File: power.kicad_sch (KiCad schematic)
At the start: 15 parts

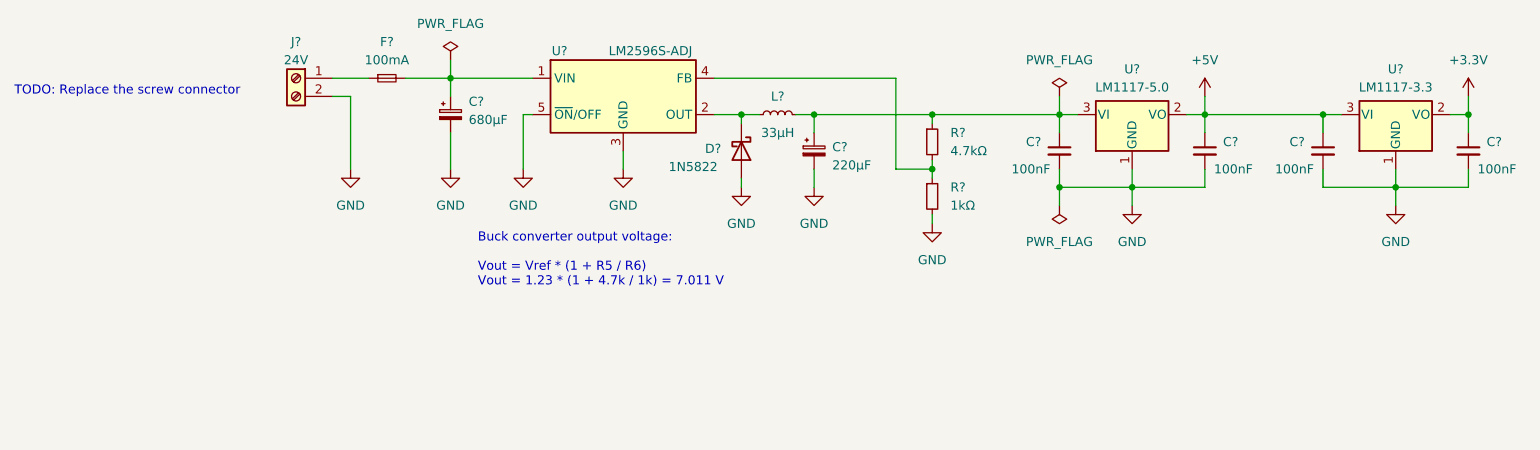
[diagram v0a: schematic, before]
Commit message: Refactor the mainboard
- Use smaller STM
- Use MPU-9250 as a motion sensor
- Connect some peripherals to the MCU
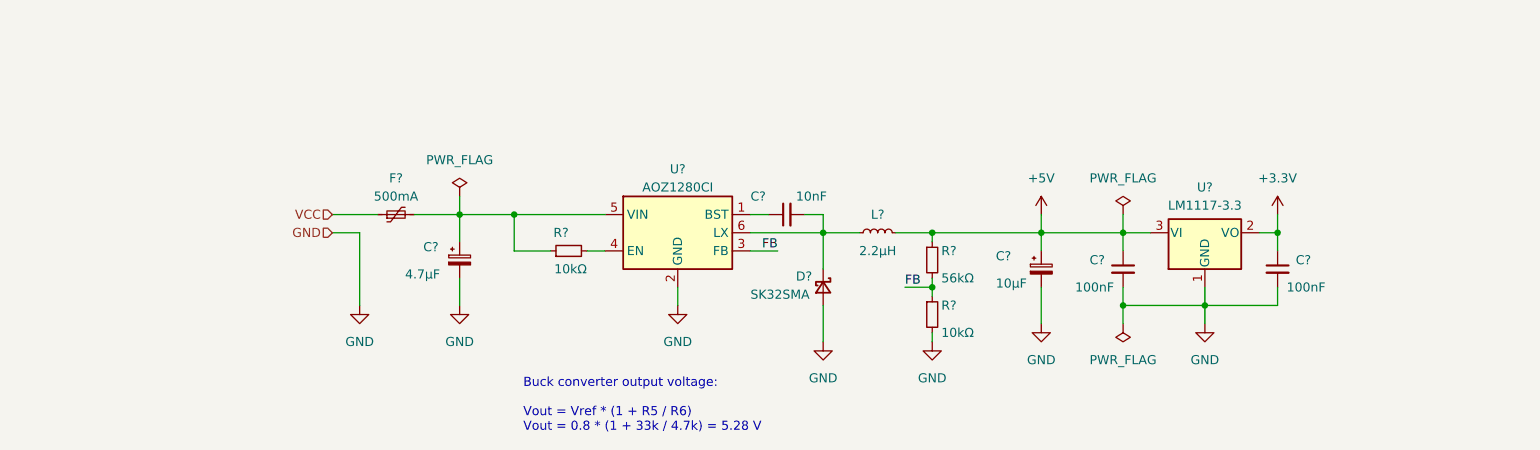
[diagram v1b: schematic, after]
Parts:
- removed C? (x4): 100nF, symbol Device:C_Small
- removed C?: 680μF, symbol Device:C_Polarized_Small
- removed C?: 220μF, symbol Device:C_Polarized_Small
- removed D?: 1N5822, Diode_THT:D_DO-201AD_P15.24mm_Horizontal, symbol Diode:1N5822
- removed F?: 100mA, symbol Device:Fuse_Small
- removed J?: 24V, symbol Connector:Screw_Terminal_01x02
- removed L?: 33μH, symbol Device:L_Small
- removed R?: 1kΩ, symbol Device:R_Small
- removed R?: 4.7kΩ, symbol Device:R_Small
- removed U?: LM1117-3.3, symbol Regulator_Linear:LM1117-3.3
- removed U?: LM2596S-ADJ, Package_TO_SOT_SMD:TO-263-5_TabPin3, symbol Regulator_Switching:LM2596S-ADJ
- removed U?: LM1117-5.0, symbol Regulator_Linear:LM1117-5.0
- added C? (x2): 100nF, Capacitor_SMD:C_0603_1608Metric, symbol Device:C_Small
- added C?: 10μF, Capacitor_SMD:C_Elec_4x5.4, symbol Device:C_Polarized_Small
- added C?: 10nF, Capacitor_SMD:C_0603_1608Metric, symbol Device:C_Small
- added C?: 4.7μF, Capacitor_SMD:C_Elec_4x5.4, symbol Device:C_Polarized_Small
- added D?: SK32SMA, Diode_SMD:D_SMA, symbol Device:D_Schottky_Small
- added F?: 500mA, Fuse:Fuse_1210_3225Metric, symbol Device:Polyfuse_Small
- added L?: 2.2μH, Inductor_SMD:L_Bourns-SRN4018, symbol Device:L_Small
- added R? (x2): 10kΩ, Resistor_SMD:R_0603_1608Metric, symbol Device:R_Small
- added R?: 56kΩ, Resistor_SMD:R_0603_1608Metric, symbol Device:R_Small
- added U?: LM1117-3.3, Package_TO_SOT_SMD:SOT-223-3_TabPin2, symbol Regulator_Linear:LM1117-3.3
- added U?: AOZ1280CI, Package_TO_SOT_SMD:SOT-23-6, symbol Regulator_Switching:AOZ1280CI
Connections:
- net +3.3V: now also C?.1, U?.2 (VO)
- net +5V: now also C?.1, C?.1, L?.2, R?.1, U?.3 (VI)
- net GND: now also C?.2, C?.2, C?.2, C?.2, D?.2 (A), R?.2, U?.1 (GND), U?.2 (GND)
- new net: C?.1, F?.2, R?.1, U?.5 (VIN)
- new net: R?.2, U?.4 (EN)
- new net: C?.1, U?.1 (BST)
- new net: C?.2, D?.1 (K), L?.1, U?.6 (LX)
- new net FB: R?.1, R?.2, U?.3 (FB)
- new net VCC: F?.1
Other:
- note added: "Buck converter output voltage: Vout = Vref * (1 + R5 / R6) Vout = 0.8 * (1 + 33k / 4.7k) = 5.28 V"
- note removed: "Buck converter output voltage: Vout = Vref * (1 + R5 / R6) Vout = 1.23 * (1 + 4.7k / 1k) = 7.011 V"
- note removed: "TODO: Replace the screw connector"

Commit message: Connect sensors to the MCU
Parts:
- added SW2: POWER, symbol Switch:SW_SPST
- gave numbers to parts that had none: 13
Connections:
- net at C13.1, R4.1, U4.5 (VIN): now also SW2.2 (B); no longer F1.2
- new net: F1.2, SW2.1 (A)
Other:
- moved on the sheet: F1

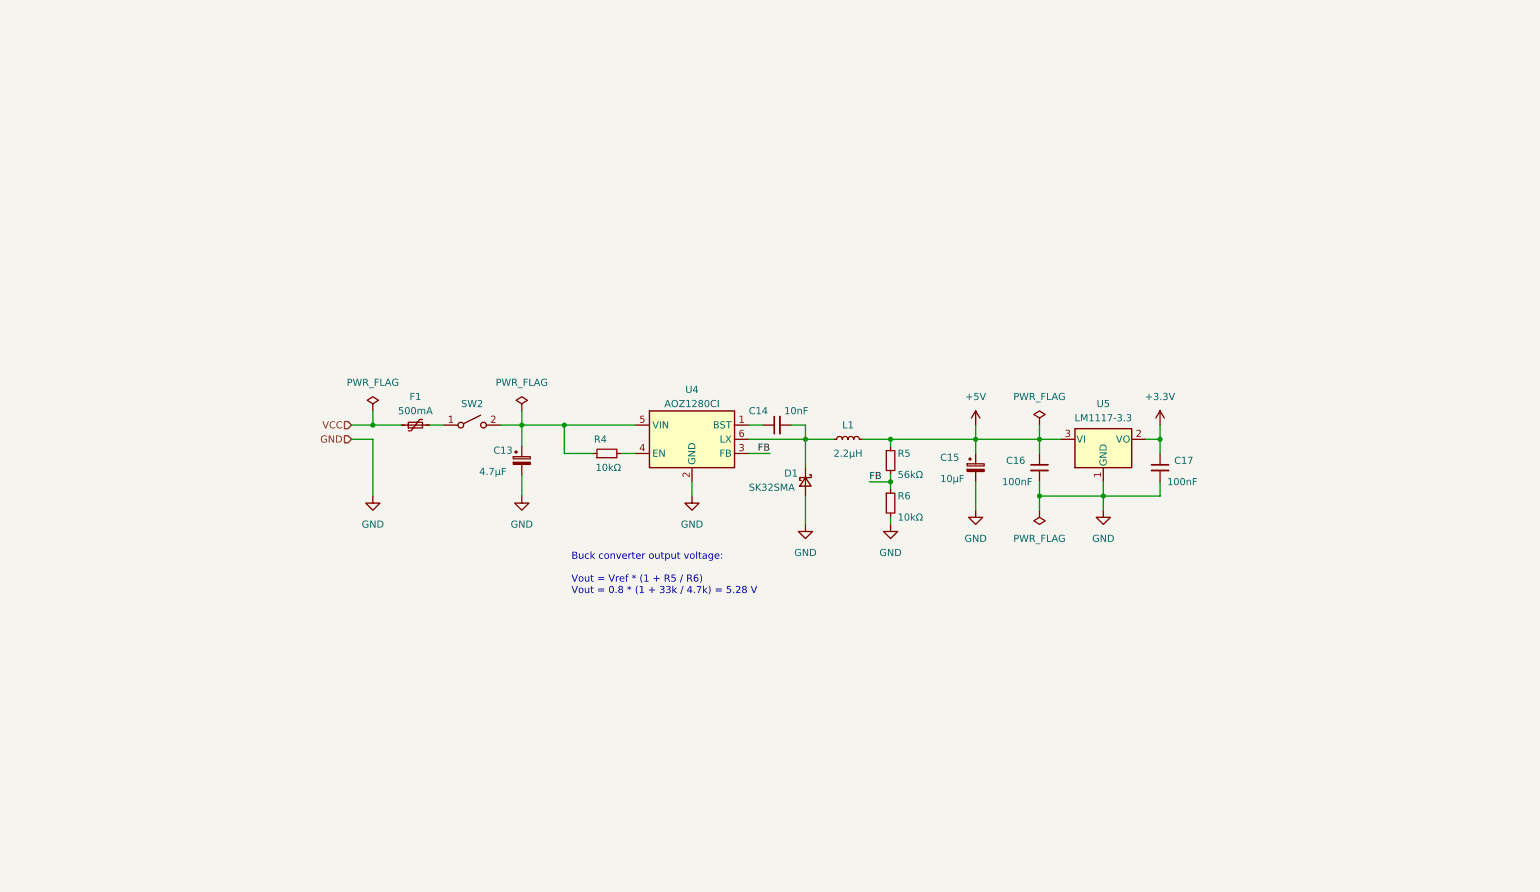
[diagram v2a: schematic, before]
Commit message: Improve the power section:
- add ADC circuit to measure battery level
- add 5V LDO regulator
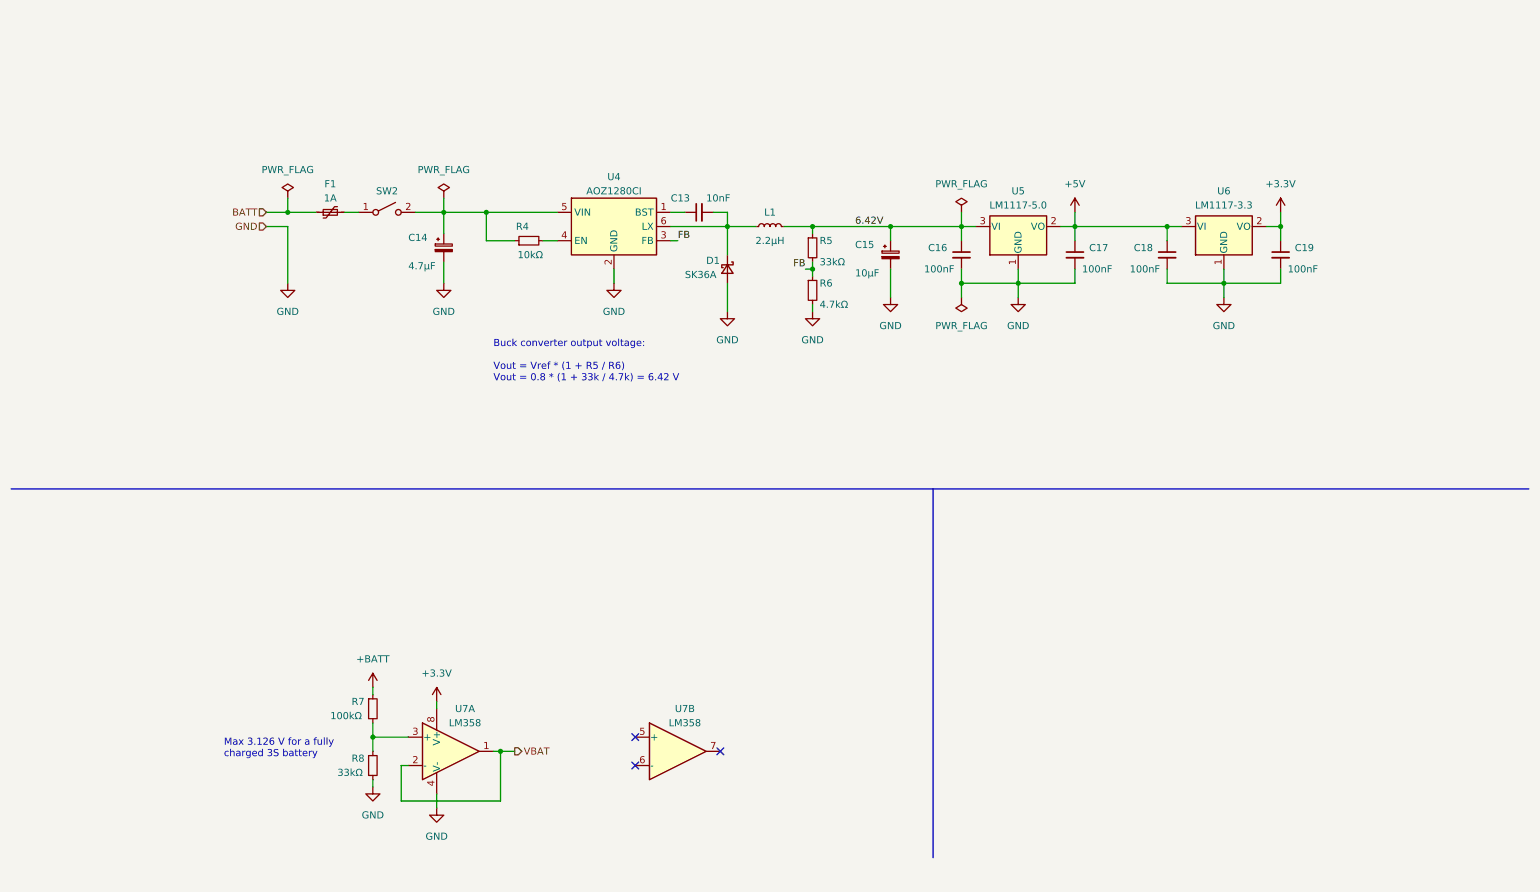
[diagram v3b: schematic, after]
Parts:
- removed C13: 4.7μF, Capacitor_SMD:C_Elec_4x5.4, symbol Device:C_Polarized_Small
- removed C14: 10nF, Capacitor_SMD:C_0603_1608Metric, symbol Device:C_Small
- removed U5: LM1117-3.3, Package_TO_SOT_SMD:SOT-223-3_TabPin2, symbol Regulator_Linear:LM1117-3.3
- added C13: 10nF, Capacitor_SMD:C_0603_1608Metric, symbol Device:C_Small
- added C14: 4.7μF, Capacitor_SMD:CP_Elec_6.3x5.4, symbol Device:C_Polarized_Small
- added C18, C19: 100nF, Capacitor_SMD:C_0603_1608Metric, symbol Device:C_Small
- added R7: 100kΩ, symbol Device:R_Small
- added R8: 33kΩ, symbol Device:R_Small
- added U5: LM1117-5.0, Package_TO_SOT_SMD:SOT-223-3_TabPin2, symbol Regulator_Linear:LM1117-5.0
- added U6: LM1117-3.3, Package_TO_SOT_SMD:SOT-223-3_TabPin2, symbol Regulator_Linear:LM1117-3.3
- added U7: LM358, symbol Amplifier_Operational:LM358
- C15: footprint Capacitor_SMD:C_Elec_4x5.4 -> Capacitor_SMD:CP_Elec_6.3x5.4
- D1: value SK32SMA -> SK36A
- F1: value 500mA -> 1A
- R5: value 56kΩ -> 33kΩ
- R6: value 10kΩ -> 4.7kΩ
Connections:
- net +3.3V: now also C19.1, U6.2 (VO), U7.8 (V+); no longer C17.1
- net +5V: now also C17.1, C18.1, U5.2 (VO), U6.3 (VI); no longer C15.1, C16.1, L1.2, R5.1
- net GND: now also C14.2, C18.2, C19.2, R8.2, U5.1 (GND), U6.1 (GND), U7.4 (V-)
- net at R4.1, SW2.2 (B), U4.5 (VIN): now also C14.1
- net at U4.1 (BST): now also C13.1
- net at D1.1 (K), L1.1, U4.6 (LX): now also C13.2
- net VCC renamed BATT
- new net: R7.2, R8.1, U7.3 (+)
- new net +BATT: R7.1
- new net 6.42V: C15.1, C16.1, L1.2, R5.1, U5.3 (VI)
- new net VBAT: U7.1, U7.2 (-)
- no-connect marks 0 -> 3
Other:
- note added: "Buck converter output voltage: Vout = Vref * (1 + R5 / R6) Vout = 0.8 * (1 + 33k / 4.7k) = 6.42 V"
- note added: "Max 3.126 V for a fully charged 3S battery"
- note removed: "Buck converter output voltage: Vout = Vref * (1 + R5 / R6) Vout = 0.8 * (1 + 33k / 4.7k) = 5.28 V"
- title: (none) -> Power Supply

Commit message: Assign footprints to symbols
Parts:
- removed SW2: POWER, symbol Switch:SW_SPST
- removed U7: LM358, symbol Amplifier_Operational:LM358
- added U5: LM358, Package_SO:SOIC-8_3.9x4.9mm_P1.27mm, symbol Amplifier_Operational:LM358
- R10: renamed from R8; footprint (none) -> Resistor_SMD:R_0603_1608Metric
- R9: renamed from R7; footprint (none) -> Resistor_SMD:R_0603_1608Metric
- renumbered C14 to C10, C15 to C11, C16 to C12, C17 to C13, C18 to C14, C19 to C15, C13 to C9, R4 to R6, R5 to R7, R6 to R8, U4 to U2, U5 to U3, U6 to U4
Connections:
- net +3.3V: now also U5.8 (V+)
- net GND: now also U5.4 (V-)
- net VBAT: now also U5.1, U5.2 (-)
- net at C10.1, R6.1, U2.5 (VIN): now also F1.2
- net at R10.1, R9.2: now also U5.3 (+)
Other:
- moved on the sheet: F1, R10, R9

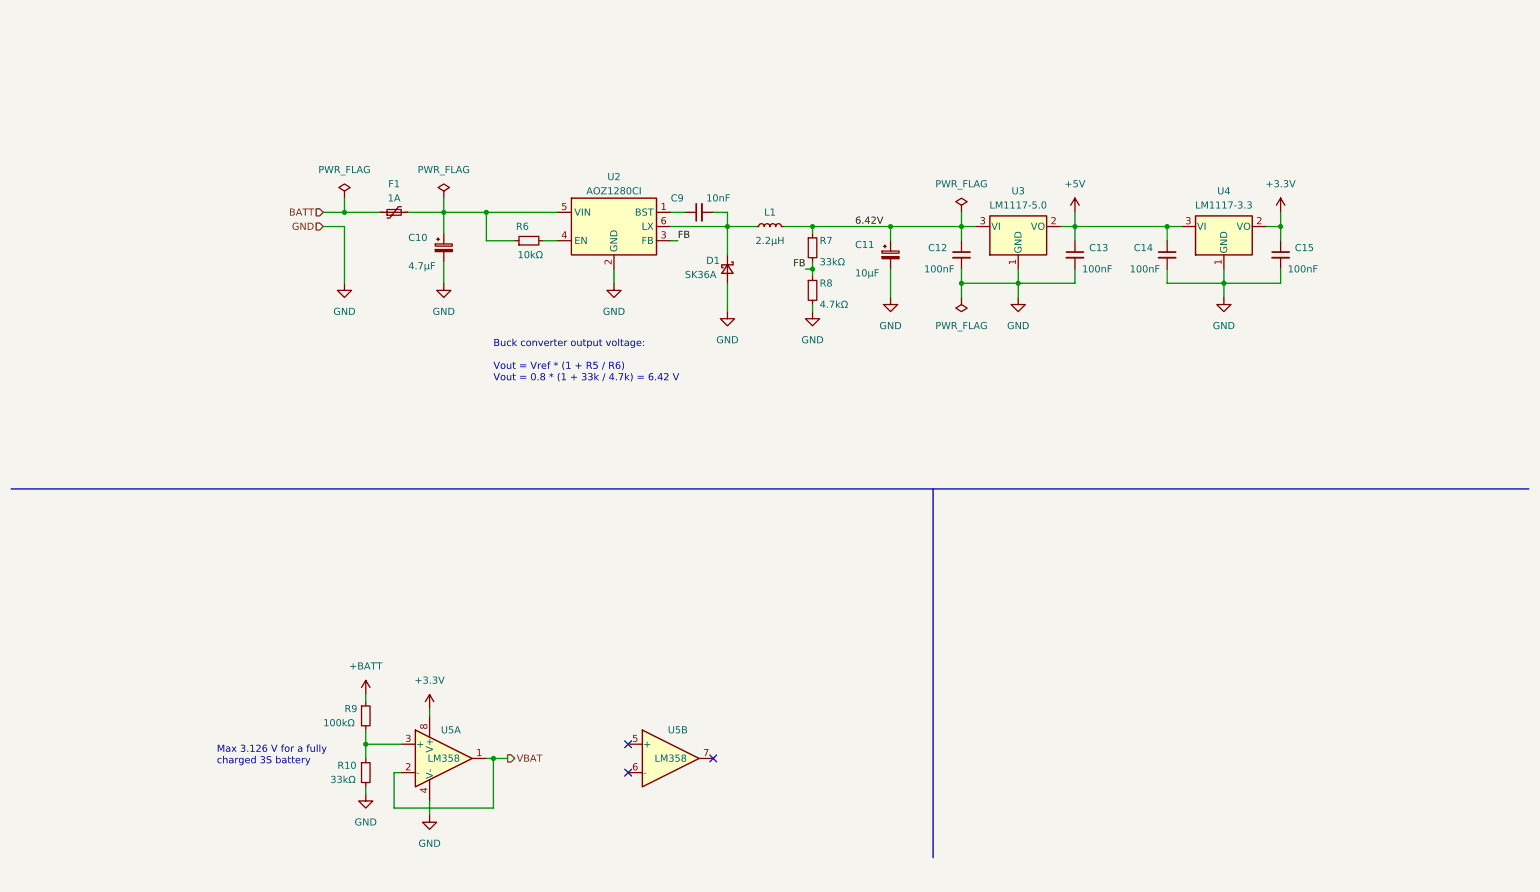
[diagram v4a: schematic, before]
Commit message: Use single connector for I/O
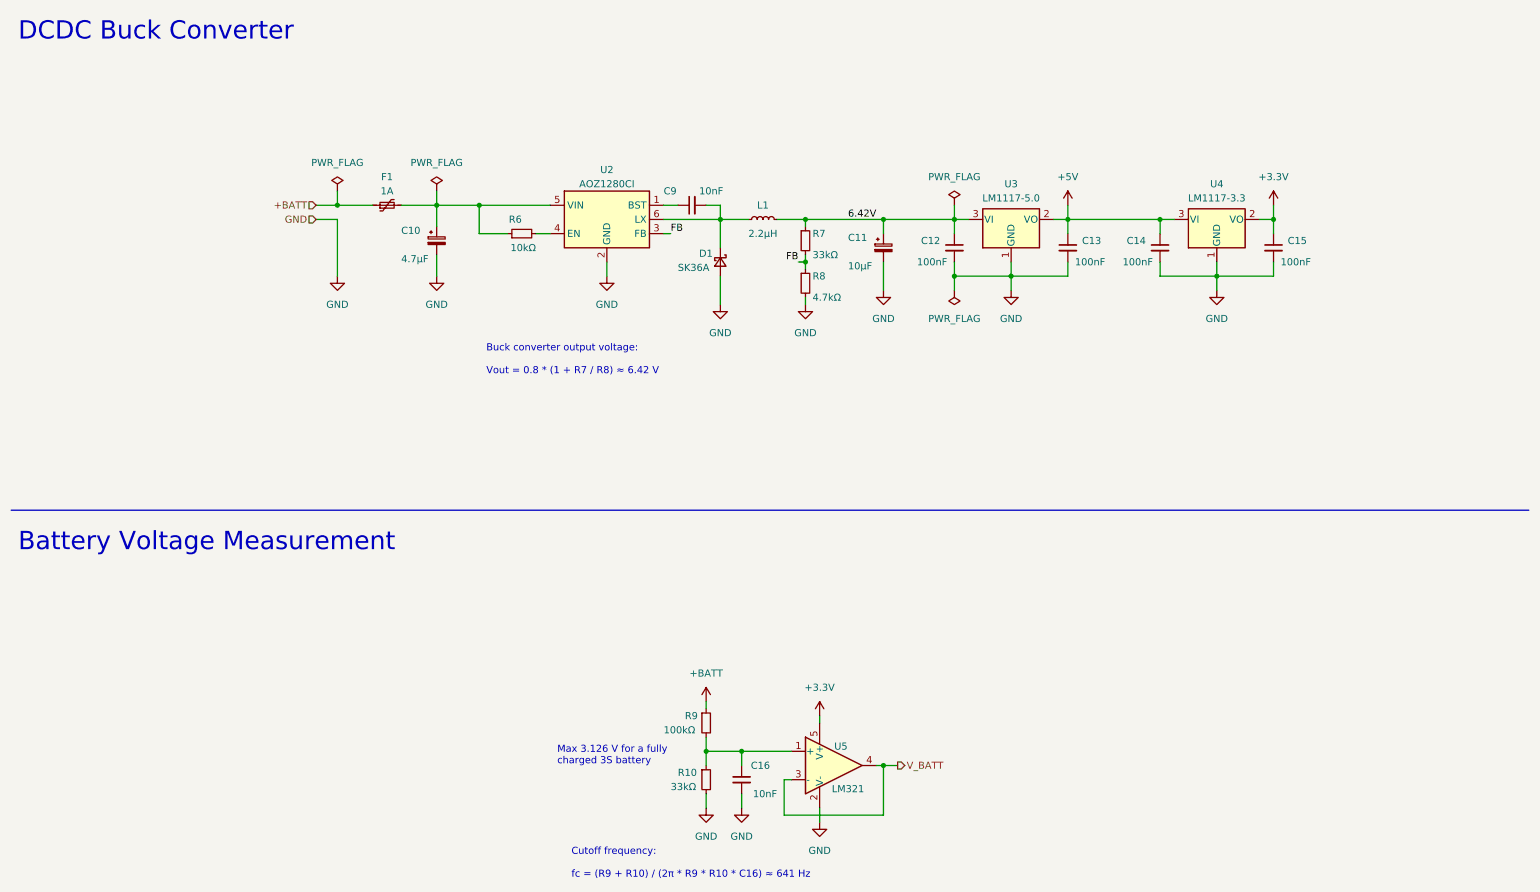
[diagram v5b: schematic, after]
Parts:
- removed U5: LM358, Package_SO:SOIC-8_3.9x4.9mm_P1.27mm, symbol Amplifier_Operational:LM358
- added C16: 10nF, Capacitor_SMD:C_0603_1608Metric, symbol Device:C_Small
- added U5: LM321, Package_TO_SOT_SMD:SOT-23-5, symbol Amplifier_Operational:LM321
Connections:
- net BATT is gone; now on net +BATT: F1.1
- net +3.3V: now also U5.5 (V+)
- net GND: now also C16.2, U5.2 (V-)
- net at R10.1, R9.2: now also C16.1, U5.1 (+)
- new net V_BATT: U5.3 (-), U5.4
- no-connect marks 3 -> 0
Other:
- note added: "Battery Voltage Measurement"
- note added: "Buck converter output voltage: Vout = 0.8 * (1 + R7 / R8) ≈ 6.42 V"
- note added: "Cutoff frequency: fc = (R9 + R10) / (2π * R9 * R10 * C16) ≈ 641 Hz"
- note added: "DCDC Buck Converter"
- note removed: "Buck converter output voltage: Vout = Vref * (1 + R5 / R6) Vout = 0.8 * (1 + 33k / 4.7k) = 6.42 V"
- moved on the sheet: C10, C11, C12, C13, C14, C15, C9, D1, F1, L1, R10, R6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
